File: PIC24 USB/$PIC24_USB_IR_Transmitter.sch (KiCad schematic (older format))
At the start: 26 parts, among them CON1 USB-MINI-B, P1 CONN_6, P2 CONN_4, P3 CONN_6, P4 CONN_6, P5 CONN_4, P6 CONN_1, P7 CONN_8, Q1 2N7002, U1 1586-PIC18F4550-I/PT, X1 12Mhz

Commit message: inserted regulator for +3v3
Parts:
- removed C3, C4: 22p, symbol C
- removed U1: 1586-PIC18F4550-I/PT, bittenbybytes/axylf, symbol 1586-PIC18F4550-I/PT
- removed X1: 12Mhz, symbol CRYSTAL
- added 10u1: C, ~, symbol C
- added U2: LM1117_SOT223_3V3, ~, symbol LM317_SOT223
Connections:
- net labels added: +3,3V
- net labels removed: OSC1, OSC2
- wire segments 131 -> 125
- no-connect marks 21 -> 4

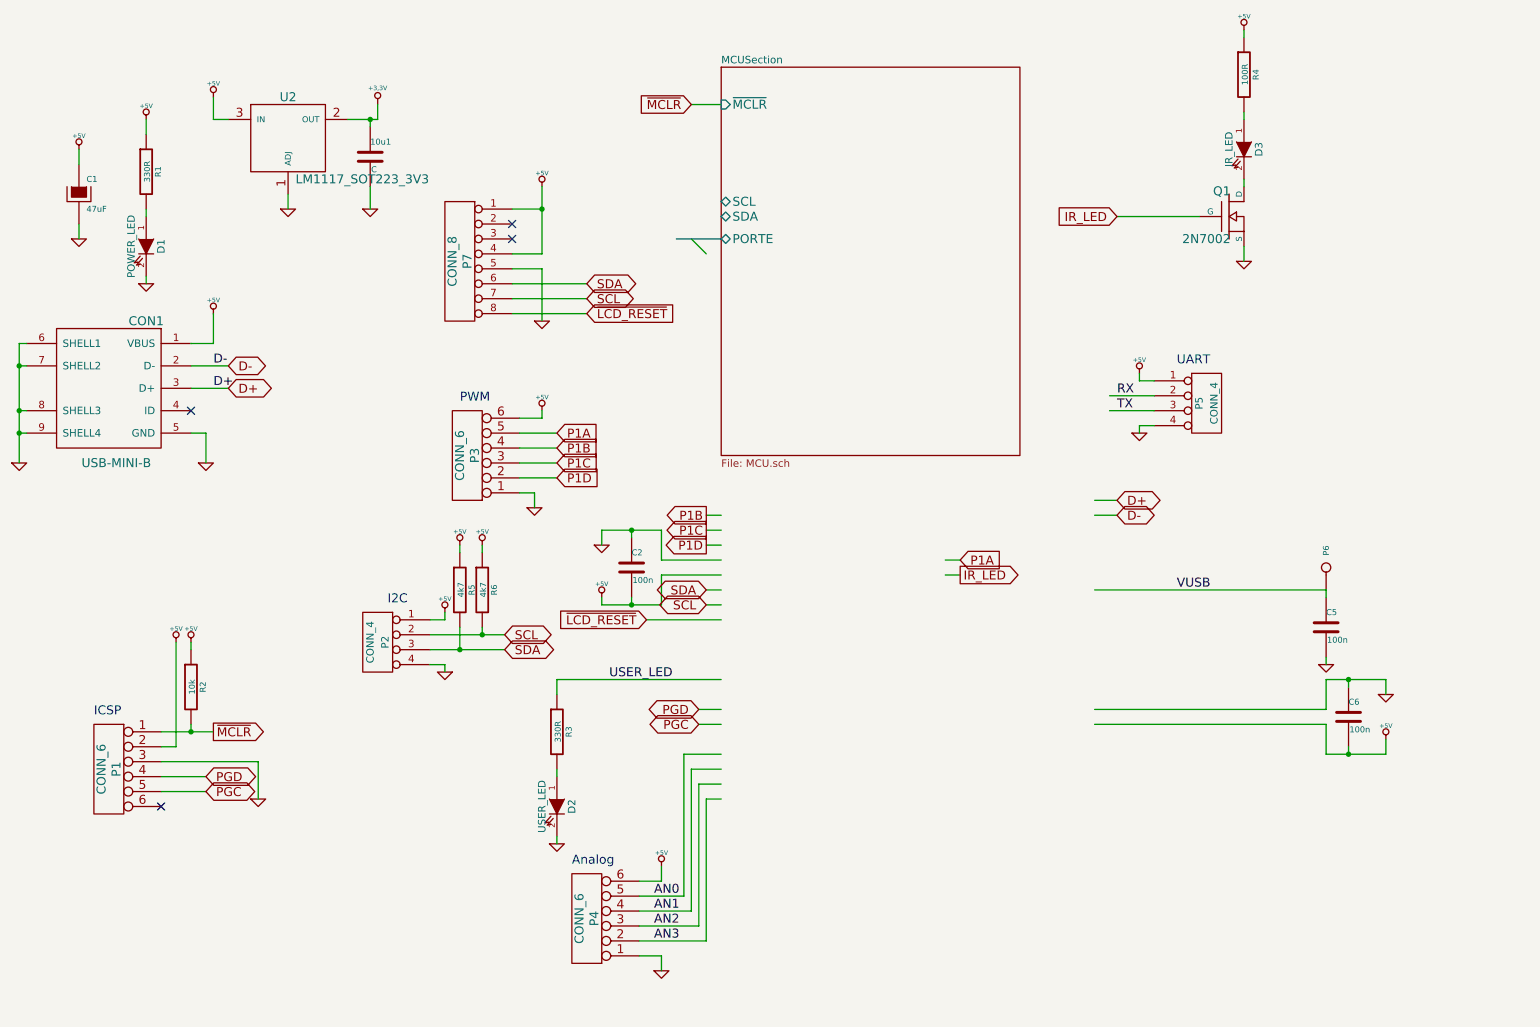
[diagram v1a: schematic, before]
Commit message: shrinked, added temp sensor, updated gerbers and submitted them
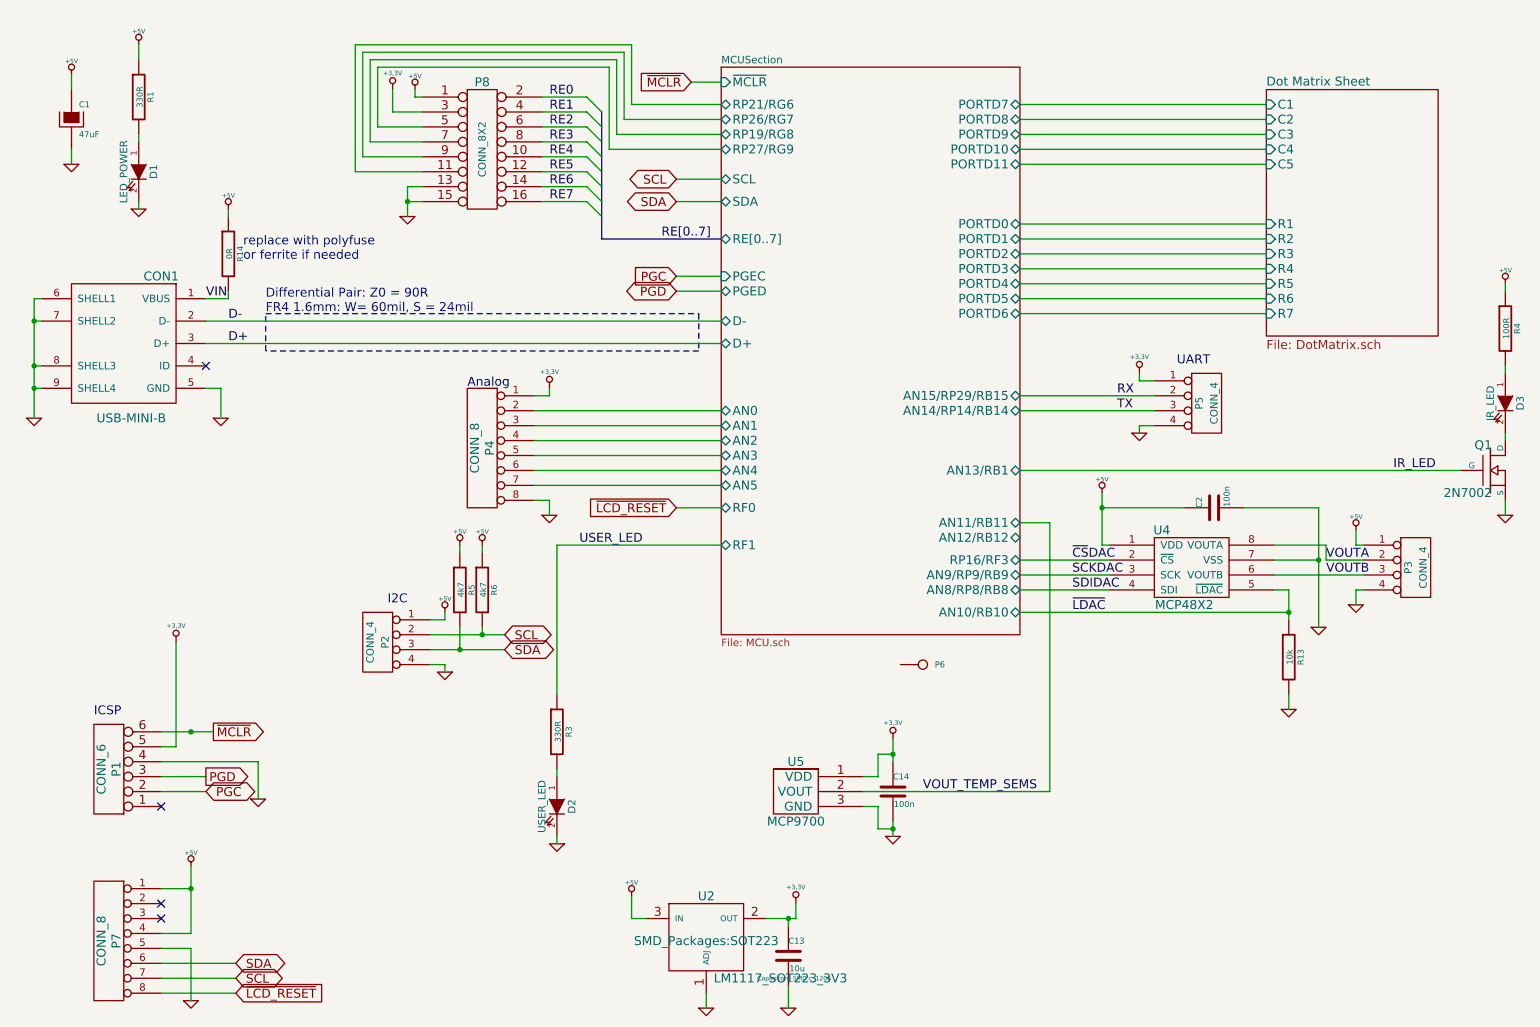
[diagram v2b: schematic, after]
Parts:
- removed C5, C6: 100n, symbol C
- removed P3, P4: CONN_6, symbol CONN_6
- removed R2: 10k, symbol R
- added C14: 100n, SMD_Packages:SMD-0603_c, symbol C
- added P3: CONN_4, Pin_Headers:Pin_Header_Straight_1x04, symbol CONN_4
- added P4: CONN_8, Pin_Headers:Pin_Header_Straight_1x08, symbol CONN_8
- added P8: CONN_8X2, Pin_Headers:Pin_Header_Straight_2x08, symbol CONN_8X2
- added R13: 10k, SMD_Packages:SMD-0603_r, symbol R
- added R14: 0R, SMD_Packages:SMD-1206, symbol R
- added U4: MCP48X2, SMD_Packages:MSOP-8, symbol MCP48X2
- added U5: MCP9700, Discret:TO92-123, symbol MCP9700
- C1: footprint (none) -> Capacitors_Tantalum_SMD:TantalC_SizeB_EIA-3528_HandSoldering
- C13: renamed from 10u1; value C -> 10u; footprint ~ -> Capacitors_SMD:c_1206
- C2: footprint (none) -> SMD_Packages:SMD-0603_c
- CON1: footprint (none) -> Connect:USB_MINI_B
- D1: value POWER_LED -> LED_POWER; footprint (none) -> LEDs:LED-0603
- D2: footprint (none) -> LEDs:LED-0603
- D3: footprint (none) -> LEDs:LED-3MM
- P1: footprint (none) -> Pin_Headers:Pin_Header_Angled_1x06
- P2, P5: footprint (none) -> Pin_Headers:Pin_Header_Straight_1x04
- P6: footprint (none) -> Symbols:Symbol_OSHW-Logo_SilkScreen
- P7: footprint (none) -> pin_array_8_50mil
- Q1: footprint (none) -> SMD_Packages:SOT-23-GDS
- R1, R3, R5, R6: footprint (none) -> SMD_Packages:SMD-0603_r
- R4: footprint (none) -> SMD_Packages:SMD-1206
- U2: footprint ~ -> SMD_Packages:SOT223
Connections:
- net labels added: RE0, RE1, RE2, RE3, RE4, RE5, RE6, RE7, RE[0..7], SCKDAC, SDIDAC, VIN, VOUTA, VOUTB, VOUT_TEMP_SEMS, ~CS~DAC, ~LDAC~
- net labels removed: AN0, AN1, AN2, AN3, P1A, P1B, P1C, P1D, VUSB
- wire segments 125 -> 159
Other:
- note added: "Differential Pair: Z0 = 90R\nFR4 1.6mm: W= 60mil, S = 24mil\n"
- note added: "replace with polyfuse\nor ferrite if needed"
- note removed: "PWM"
- moved on the sheet: C1, C13, C2, D1, D3, P7, Q1, R1, R4, U2
